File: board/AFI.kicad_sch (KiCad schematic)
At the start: 0 parts

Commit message: Added Parts, Renamed Parts
Added in switches, buttons, & multiple anderson connections for power.
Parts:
- added Conn7: AndersonPP, symbol MRDT_Connectors:AndersonPP
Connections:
- new net +12V: Conn7.2 (V+Log)
- new net GND: Conn7.1 (GND)

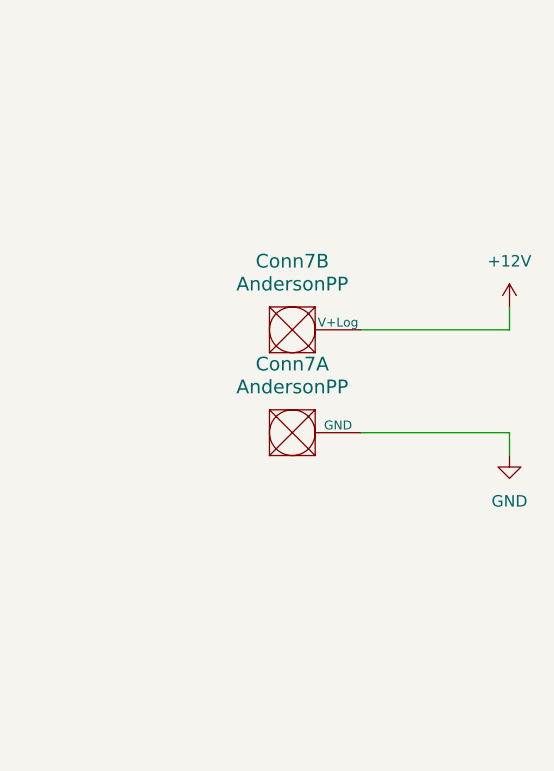
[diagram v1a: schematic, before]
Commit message: Added Labels, Missing Requirements, and Refined Look
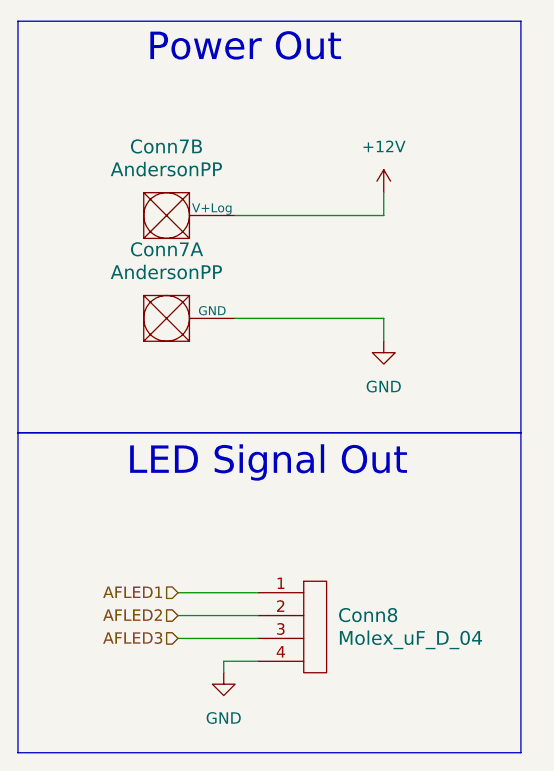
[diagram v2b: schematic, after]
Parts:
- added Conn8: Molex_uF_D_04, MRDT_Connectors:MOLEX_uF_D_04_Horizontal, symbol MRDT_Connectors:Molex_uF_D_04
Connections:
- net GND: now also Conn8.4
- new net AFLED1: Conn8.1
- new net AFLED2: Conn8.2
- new net AFLED3: Conn8.3
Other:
- note added: "LED Signal Out"
- note added: "Power Out"
- moved on the sheet: Conn7A, Conn7B

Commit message: Adjusted resistor values & renamed AF outputs
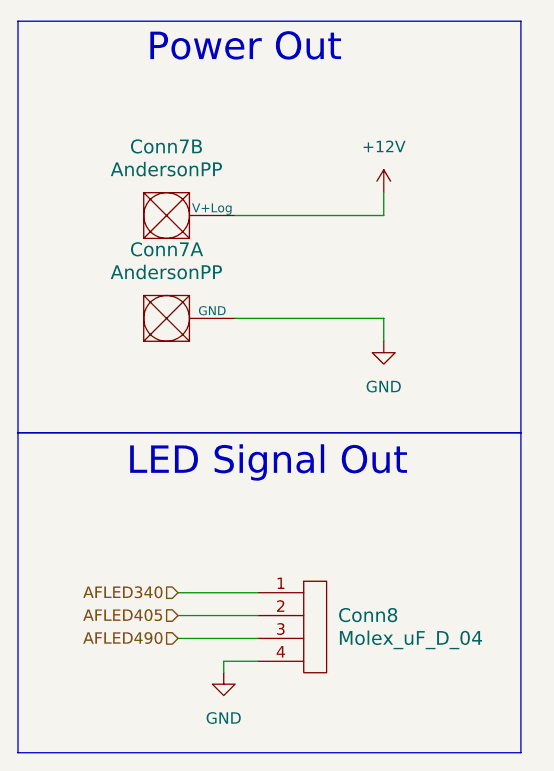
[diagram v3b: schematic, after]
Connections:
- net AFLED1 renamed AFLED340
- net AFLED2 renamed AFLED405
- net AFLED3 renamed AFLED490
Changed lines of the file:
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@@
 		)
 	)
-	(hierarchical_label "AFLED2"
+	(hierarchical_label "AFLED405"
 		(shape input)
 		(at 30.48 78.74 180)
@@
 		)
 	)
-	(hierarchical_label "AFLED3"
+	(hierarchical_label "AFLED490"
 		(shape input)
 		(at 30.48 81.28 180)
@@
 		)
 	)
-	(hierarchical_label "AFLED1"
+	(hierarchical_label "AFLED340"
 		(shape input)
 		(at 30.48 76.2 180)

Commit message: assigned footprints
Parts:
- Conn7: footprint (none) -> MRDT_Connectors:Square_Anderson_2_H_Side_By_Side_PV
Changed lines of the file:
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@@
 			)
 		)
-		(property "Footprint" ""
+		(property "Footprint" "MRDT_Connectors:Square_Anderson_2_H_Side_By_Side_PV"
 			(at 22.86 50.8 0)
 			(effects
@@
 			)
 		)
-		(property "Footprint" ""
+		(property "Footprint" "MRDT_Connectors:Square_Anderson_2_H_Side_By_Side_PV"
 			(at 22.86 62.23 0)
 			(effects

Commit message: switched soil sensor ports and layout work
soil sensor ports in fact needed to be the way they were originally after looking into the sensors we are using. Also started moving different components on layout to their spots.
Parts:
- Conn8: footprint MRDT_Connectors:MOLEX_uF_D_04_Horizontal -> MRDT_Connectors:MOLEX_SL_04_Vertical
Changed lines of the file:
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@@
 			)
 		)
-		(property "Footprint" "MRDT_Connectors:MOLEX_uF_D_04_Horizontal"
+		(property "Footprint" "MRDT_Connectors:MOLEX_SL_04_Vertical"
 			(at 44.45 85.09 0)
 			(effects

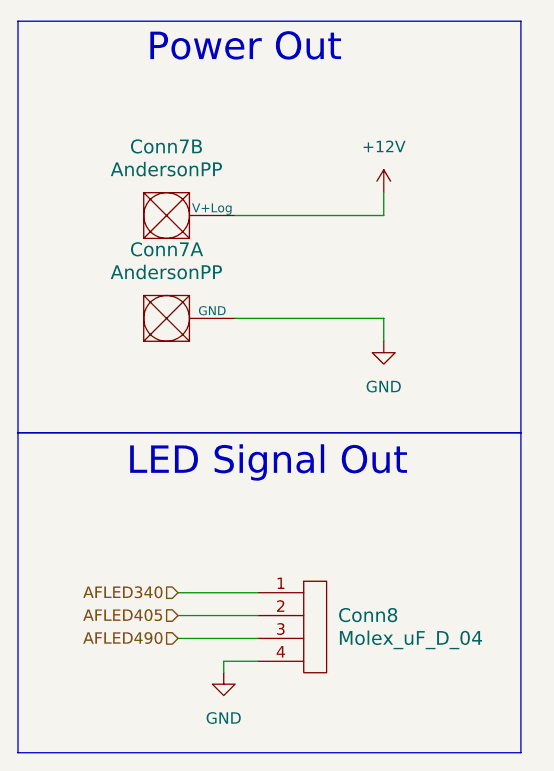
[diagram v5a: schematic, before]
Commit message: Redid layout to shrink & add new power connectors
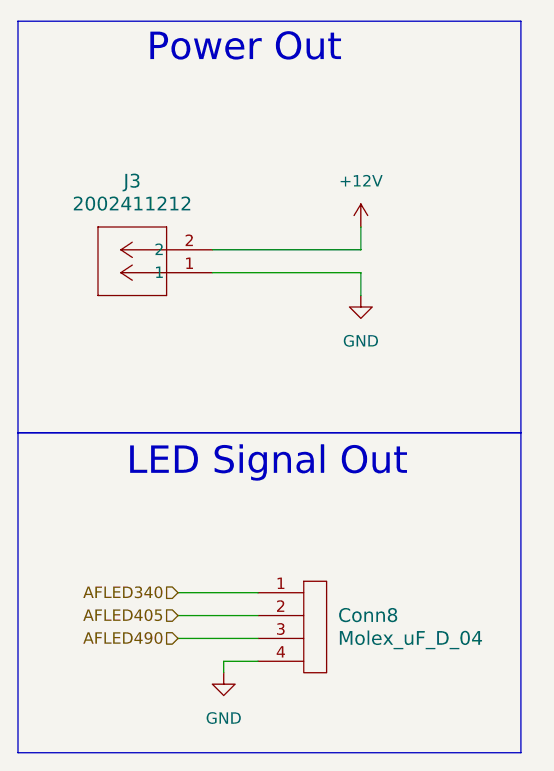
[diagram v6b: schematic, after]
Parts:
- removed Conn7: AndersonPP, MRDT_Connectors:Square_Anderson_2_H_Side_By_Side_PV, symbol MRDT_Connectors:AndersonPP
- added J3: 2002411212, footprints:CONN_2002412000_02_MOL, symbol 2025-11-04_23-05-57:2002411212
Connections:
- net +12V: now also J3.2
- net GND: now also J3.1
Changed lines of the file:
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@@
 	(wire
 		(pts
-			(xy 53.34 45.72) (xy 36.83 45.72)
+			(xy 50.8 40.64) (xy 34.29 40.64)
 		)
 		(stroke
@@
 	(wire
 		(pts
-			(xy 53.34 31.75) (xy 53.34 34.29)
-		)
-		(stroke
-			(width 0)
-			(type default)
-		)
-	)
-	(wire
-		(pts
-			(xy 53.34 34.29) (xy 36.83 34.29)
+			(xy 50.8 35.56) (xy 50.8 38.1)
+		)
+		(stroke
+			(width 0)
+			(type default)
+		)
+	)
+	(wire
+		(pts
+			(xy 50.8 38.1) (xy 34.29 38.1)
 		)
 		(stroke
@@
 	(wire
 		(pts
-			(xy 53.34 48.26) (xy 53.34 45.72)
+			(xy 50.8 43.18) (xy 50.8 40.64)
 		)
 		(stroke
@@
 	)
 	(symbol
-		(lib_id "MRDT_Connectors:AndersonPP")
-		(at 26.67 36.83 0)
-		(unit 2)
+		(lib_id "2025-11-04_23-05-57:2002411212")
+		(at 34.29 40.64 180)
+		(unit 1)
 		(exclude_from_sim no)
 		(in_bom yes)
@@
 		(dnp no)
 		(fields_autoplaced yes)
-		(property "Reference" "Conn7"
-			(at 29.21 26.67 0)
+		(property "Reference" "J3"
+			(at 25.4 30.48 0)
 			(effects
 				(font
@@
 			)
 		)
-		(property "Value" "AndersonPP"
-			(at 29.21 29.21 0)
+		(property "Value" "2002411212"
+			(at 25.4 33.02 0)
 			(effects
 				(font
@@
 			)
 		)
-		(property "Footprint" "MRDT_Connectors:Square_Anderson_2_H_Side_By_Side_PV"
-			(at 22.86 50.8 0)
-			(effects
-				(font
-					(size 1.524 1.524)
-				)
-				(hide yes)
-			)
-		)
-		(property "Datasheet" ""
-			(at 22.86 50.8 0)
-			(effects
-				(font
-					(size 1.524 1.524)
+		(property "Footprint" "footprints:CONN_2002412000_02_MOL"
+			(at 34.29 40.64 0)
+			(effects
+				(font
+					(size 1.27 1.27)
+					(italic yes)
+				)
+				(hide yes)
+			)
+		)
+		(property "Datasheet" "https://www.molex.com/en-us/products/part-detail-pdf/2002411212?display=pdf"
+			(at 34.29 40.64 0)
+			(effects
+				(font
+					(size 1.27 1.27)
+					(italic yes)
 				)
 				(hide yes)
@@
 		)
 		(property "Description" ""
-			(at 26.67 36.83 0)
-			(effects
-				(font
-					(size 1.27 1.27)
-				)
-				(hide yes)
-			)
+			(at 34.29 40.64 0)
+			(effects
+				(font
+					(size 1.27 1.27)
+				)
+				(hide yes)
+			)
+		)
+		(pin "1"
 		)
 		(pin "2"
 		)
-		(pin "1"
-		)
-		(pin "1"
-		)
-		(pin "4"
-		)
-		(pin "3"
-		)
 		(instances
-			(project "AugerBoard"
+			(project ""
 				(path "/05fd3c2e-b986-4426-9c38-2a77d5c929de/874d0dfc-2f90-4409-9fd5-46a48fc81ade"
-					(reference "Conn7")
-					(unit 2)
+					(reference "J3")
+					(unit 1)
 				)
 			)
@@
 	(symbol
 		(lib_id "power:+12V")
-		(at 53.34 31.75 0)
+		(at 50.8 35.56 0)
 		(unit 1)
 		(exclude_from_sim no)
@@
 		(fields_autoplaced yes)
 		(property "Reference" "#PWR030"
-			(at 53.34 35.56 0)
+			(at 50.8 39.37 0)
 			(effects
 				(font
@@
 		)
 		(property "Value" "+12V"
-			(at 53.34 26.67 0)
+			(at 50.8 30.48 0)
 			(effects
 				(font
@@
 		)
 		(property "Footprint" ""
-			(at 53.34 31.75 0)
+			(at 50.8 35.56 0)
 			(effects
 				(font
@@
 		)
 		(property "Datasheet" ""
-			(at 53.34 31.75 0)
+			(at 50.8 35.56 0)
 			(effects
 				(font
@@
 		)
 		(property "Description" "Power symbol creates a global label with name \"+12V\""
-			(at 53.34 31.75 0)
+			(at 50.8 35.56 0)
 			(effects
 				(font
@@
 	)
 	(symbol
-		(lib_id "MRDT_Connectors:AndersonPP")
-		(at 26.67 48.26 0)
-		(unit 1)
-		(exclude_from_sim no)
-		(in_bom yes)
-		(on_board yes)
-		(dnp no)
-		(fields_autoplaced yes)
-		(property "Reference" "Conn7"
-			(at 29.21 38.1 0)
-			(effects
-				(font
-					(size 1.524 1.524)
-				)
-			)
-		)
-		(property "Value" "AndersonPP"
-			(at 29.21 40.64 0)
-			(effects
-				(font
-					(size 1.524 1.524)
-				)
-			)
-		)
-		(property "Footprint" "MRDT_Connectors:Square_Anderson_2_H_Side_By_Side_PV"
-			(at 22.86 62.23 0)
-			(effects
-				(font
-					(size 1.524 1.524)
-				)
-				(hide yes)
-			)
-		)
-		(property "Datasheet" ""
-			(at 22.86 62.23 0)
-			(effects
-				(font
-					(size 1.524 1.524)
-				)
-				(hide yes)
-			)
-		)
-		(property "Description" ""
-			(at 26.67 48.26 0)
-			(effects
-				(font
-					(size 1.27 1.27)
-				)
-				(hide yes)
-			)
-		)
-		(pin "2"
-		)
-		(pin "1"
-		)
-		(pin "1"
-		)
-		(pin "4"
-		)
-		(pin "3"
-		)
-		(instances
-			(project "AugerBoard"
-				(path "/05fd3c2e-b986-4426-9c38-2a77d5c929de/874d0dfc-2f90-4409-9fd5-46a48fc81ade"
-					(reference "Conn7")
-					(unit 1)
-				)
-			)
-		)
-	)
-	(symbol
 		(lib_id "power:GND")
-		(at 53.34 48.26 0)
+		(at 50.8 43.18 0)
 		(unit 1)
 		(exclude_from_sim no)
@@
 		(fields_autoplaced yes)
 		(property "Reference" "#PWR043"
-			(at 53.34 54.61 0)
+			(at 50.8 49.53 0)
 			(effects
 				(font
@@
 		)
 		(property "Value" "GND"
-			(at 53.34 53.34 0)
+			(at 50.8 48.26 0)
 			(effects
 				(font
@@
 		)
 		(property "Footprint" ""
-			(at 53.34 48.26 0)
+			(at 50.8 43.18 0)
 			(effects
 				(font
@@
 		)
 		(property "Datasheet" ""
-			(at 53.34 48.26 0)
+			(at 50.8 43.18 0)
 			(effects
 				(font
@@
 		)
 		(property "Description" "Power symbol creates a global label with name \"GND\" , ground"
-			(at 53.34 48.26 0)
-			(effects
-				(font
+			(at 50.8 43.18 0)
+			(effects
+				(font

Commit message: fine tuning
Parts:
- J3: footprint footprints:CONN_2002412000_02_MOL -> footprints:CONN_SD-76825-0100_02_MOL
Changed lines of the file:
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@@
 			)
 		)
-		(property "Footprint" "footprints:CONN_2002412000_02_MOL"
+		(property "Footprint" "footprints:CONN_SD-76825-0100_02_MOL"
 			(at 34.29 40.64 0)
 			(effects

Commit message: added pin for AF, added gimbal names, refined look
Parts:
- removed Conn8: Molex_uF_D_04, MRDT_Connectors:MOLEX_SL_04_Vertical, symbol MRDT_Connectors:Molex_uF_D_04
- added Conn1: Molex_SL_05, MRDT_Connectors:MOLEX_SL_05_Vertical, symbol MRDT_Connectors:Molex_SL_05
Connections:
- net AFLED340: now also Conn1.1
- net AFLED405: now also Conn1.2
- net AFLED490: now also Conn1.3
- net GND: now also Conn1.5
- new net AFWhiteLED: Conn1.4
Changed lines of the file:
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@@
+	(wire
+		(pts
+			(xy 35.56 86.36) (xy 39.37 86.36)
+		)
+		(stroke
+			(width 0)
+			(type default)
+		)
+	)
 	(wire
 		(pts
@@
 	(wire
 		(pts
-			(xy 35.56 85.09) (xy 35.56 83.82)
+			(xy 35.56 87.63) (xy 35.56 86.36)
 		)
 		(stroke
@@
 	(wire
 		(pts
+			(xy 30.48 83.82) (xy 39.37 83.82)
+		)
+		(stroke
+			(width 0)
+			(type default)
+		)
+	)
+	(wire
+		(pts
 			(xy 30.48 76.2) (xy 39.37 76.2)
 		)
@@
 	(wire
 		(pts
-			(xy 35.56 83.82) (xy 39.37 83.82)
-		)
-		(stroke
-			(width 0)
-			(type default)
-		)
-	)
-	(wire
-		(pts
 			(xy 50.8 43.18) (xy 50.8 40.64)
 		)
@@
 			(width 0)
 			(type default)
+		)
+	)
+	(hierarchical_label "AFWhiteLED"
+		(shape input)
+		(at 30.48 83.82 180)
+		(effects
+			(font
+				(size 1.27 1.27)
+			)
+			(justify right)
 		)
 	)
@@
 	)
 	(symbol
-		(lib_id "MRDT_Connectors:Molex_uF_D_04")
-		(at 44.45 85.09 0)
-		(unit 1)
-		(exclude_from_sim no)
-		(in_bom yes)
-		(on_board yes)
-		(dnp no)
-		(fields_autoplaced yes)
-		(property "Reference" "Conn8"
-			(at 48.26 78.7399 0)
-			(effects
-				(font
-					(size 1.524 1.524)
-				)
-				(justify left)
-			)
-		)
-		(property "Value" "Molex_uF_D_04"
-			(at 48.26 81.2799 0)
-			(effects
-				(font
-					(size 1.524 1.524)
-				)
-				(justify left)
-			)
-		)
-		(property "Footprint" "MRDT_Connectors:MOLEX_SL_04_Vertical"
-			(at 44.45 85.09 0)
-			(effects
-				(font
-					(size 1.524 1.524)
-				)
-				(hide yes)
-			)
-		)
-		(property "Datasheet" ""
-			(at 44.45 85.09 0)
-			(effects
-				(font
-					(size 1.524 1.524)
-				)
-				(hide yes)
-			)
-		)
-		(property "Description" ""
-			(at 44.45 85.09 0)
-			(effects
-				(font
-					(size 1.27 1.27)
-				)
-				(hide yes)
-			)
-		)
-		(pin "2"
-		)
-		(pin "3"
-		)
-		(pin "4"
-		)
-		(pin "1"
-		)
-		(instances
-			(project ""
-				(path "/05fd3c2e-b986-4426-9c38-2a77d5c929de/874d0dfc-2f90-4409-9fd5-46a48fc81ade"
-					(reference "Conn8")
-					(unit 1)
-				)
-			)
-		)
-	)
-	(symbol
 		(lib_id "power:GND")
-		(at 35.56 85.09 0)
+		(at 35.56 87.63 0)
 		(unit 1)
 		(exclude_from_sim no)
@@
 		(fields_autoplaced yes)
 		(property "Reference" "#PWR057"
-			(at 35.56 91.44 0)
+			(at 35.56 93.98 0)
 			(effects
 				(font
@@
 		)
 		(property "Value" "GND"
-			(at 35.56 90.17 0)
+			(at 35.56 92.71 0)
 			(effects
 				(font
@@
 		)
 		(property "Footprint" ""
-			(at 35.56 85.09 0)
+			(at 35.56 87.63 0)
 			(effects
 				(font
@@
 		)
 		(property "Datasheet" ""
-			(at 35.56 85.09 0)
+			(at 35.56 87.63 0)
 			(effects
 				(font
@@
 		)
 		(property "Description" "Power symbol creates a global label with name \"GND\" , ground"
-			(at 35.56 85.09 0)
+			(at 35.56 87.63 0)
 			(effects
 				(font
@@
 					(unit 1)
 				)
+			)
+		)
+	)
+	(symbol
+		(lib_id "MRDT_Connectors:Molex_SL_05")
+		(at 44.45 87.63 0)
+		(unit 1)
+		(exclude_from_sim no)
+		(in_bom yes)
+		(on_board yes)
+		(dnp no)
+		(fields_autoplaced yes)
+		(property "Reference" "Conn1"
+			(at 48.26 80.0099 0)
+			(effects
+				(font
+					(size 1.524 1.524)
+				)
+				(justify left)
+			)
+		)
+		(property "Value" "Molex_SL_05"
+			(at 48.26 82.5499 0)
+			(effects
+				(font
+					(size 1.524 1.524)
+				)
+				(justify left)
+			)
+		)
+		(property "Footprint" "MRDT_Connectors:MOLEX_SL_05_Vertical"
+			(at 44.45 87.63 0)
+			(effects
+				(font
+					(size 1.524 1.524)
+				)
+				(hide yes)
+			)
+		)
+		(property "Datasheet" ""
+			(at 44.45 87.63 0)
+			(effects
+				(font
+					(size 1.524 1.524)
+				)
+				(hide yes)
+			)
+		)
+		(property "Description" ""
+			(at 44.45 87.63 0)
+			(effects
+				(font
+					(size 1.27 1.27)
+				)
+				(hide yes)
+			)
+		)
+		(pin "5"
+		)
+		(pin "4"
+		)
+		(pin "2"
+		)
+		(pin "1"
+		)
+		(pin "3"
+		)
+		(instances
+			(project ""
+				(path "/05fd3c2e-b986-4426-9c38-2a77d5c929de/874d0dfc-2f90-4409-9fd5-46a48fc81ade"
+					(reference "Conn1")
+					(unit 1)
+				)
